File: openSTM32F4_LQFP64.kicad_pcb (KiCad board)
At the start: 2 copper layers, 54 x 68 mm, 77 parts, among them J1 Barrel_Jack_Switch, J10 Conn_01x04, J11 Conn_01x04, J12 Conn_01x05, J13 USB_B_Micro, J14 Conn_01x04, J15 Conn_01x04, J16 Conn_01x05, J17 Conn_01x06, J18 Conn_01x04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

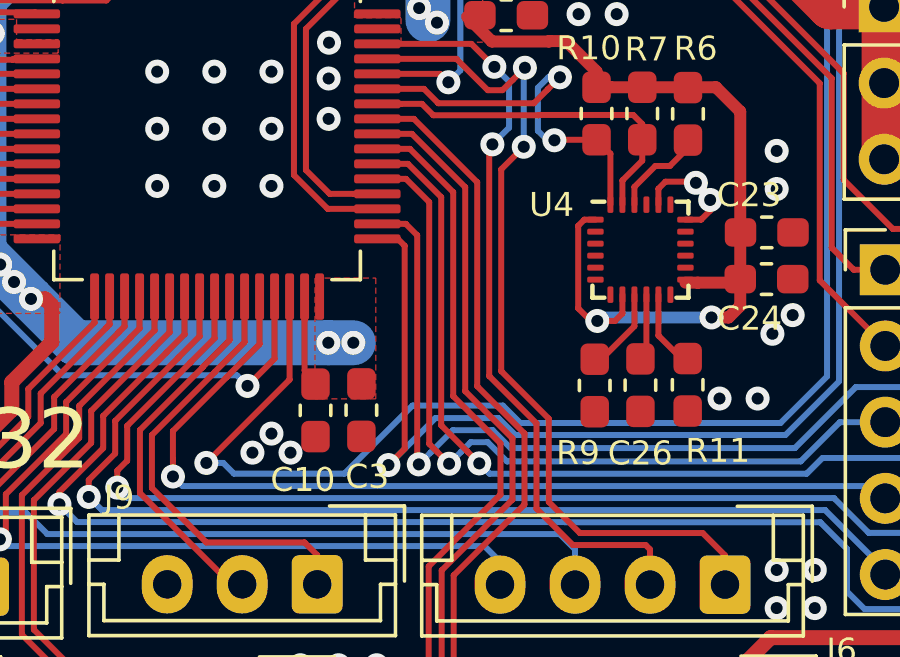
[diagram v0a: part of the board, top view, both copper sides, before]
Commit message: update mpu9250 footprint
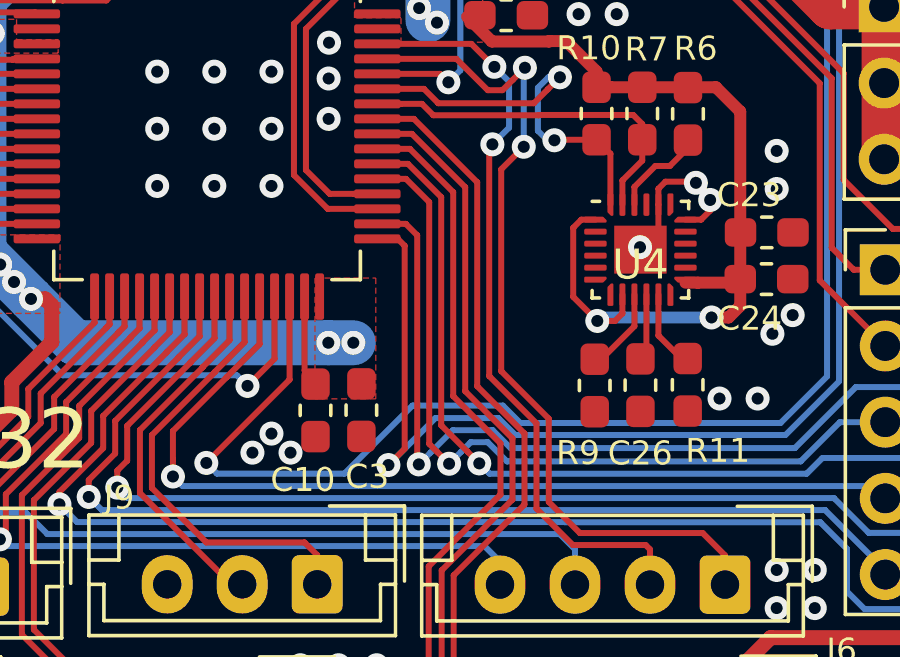
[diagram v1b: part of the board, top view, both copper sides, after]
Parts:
- U4: footprint Sensor_Motion:InvenSense_QFN-24_3x3mm_P0.4mm -> footprints:MPU9250
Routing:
- net GND: track 3.24 -> 4.99 mm, vias 196 -> 197
